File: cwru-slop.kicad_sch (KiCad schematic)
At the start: 58 parts, among them J1 USB_C_Receptacle_USB2.0_16P, J2 FTSH-105-01-L-DV-007-K, J3 Conn_01x03_Pin, J4 54-00320, U1 TLV9001IDCK, U10 B3U-1000P, U11 TLV9001IDCK, U12 TLV9001IDCK, U2 AP63205WU, U3 TLV75533PDBV, U4 STM32L433CCTx, U5 TPS2116DRL, U6 FXLS8974CFR3, U7 ESDCAN24-2BLY, U8 MCP2562-E-SN, U9 24lc32at-i/ot, Y1 XRCGB24M000F3M00R0

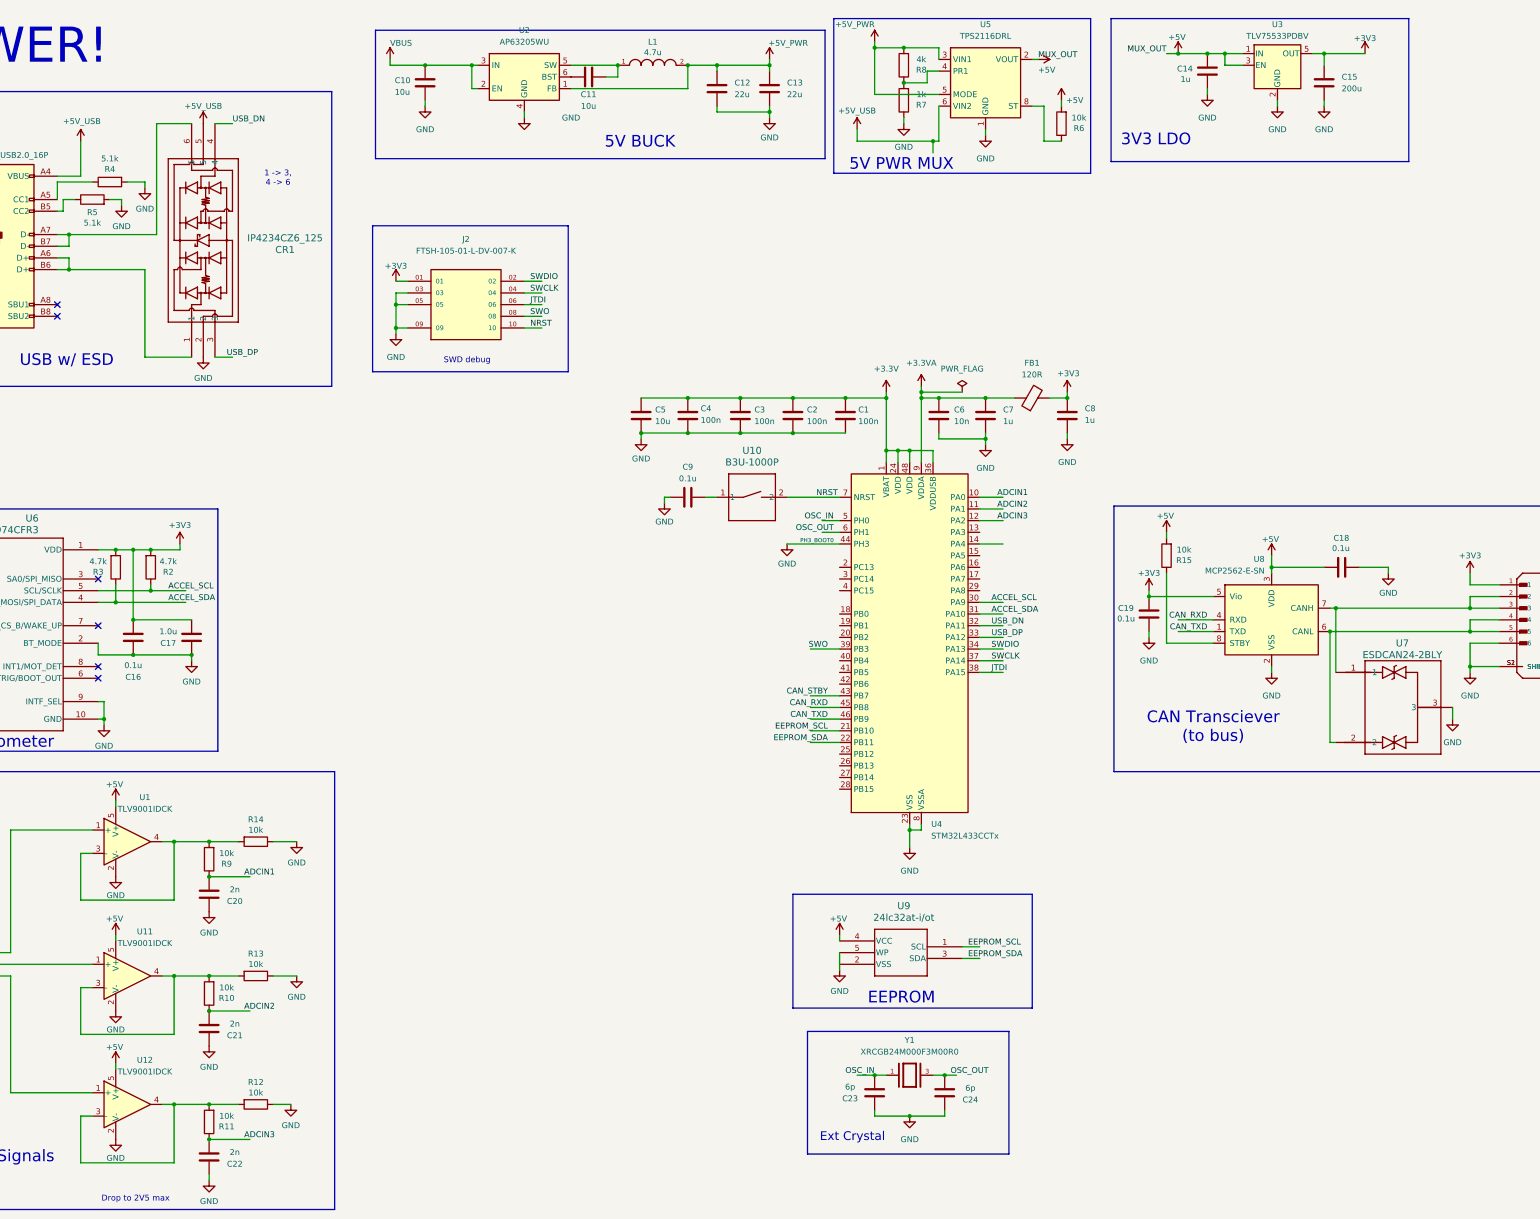
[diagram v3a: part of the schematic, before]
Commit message: add led, pull-ups, clean up a bit
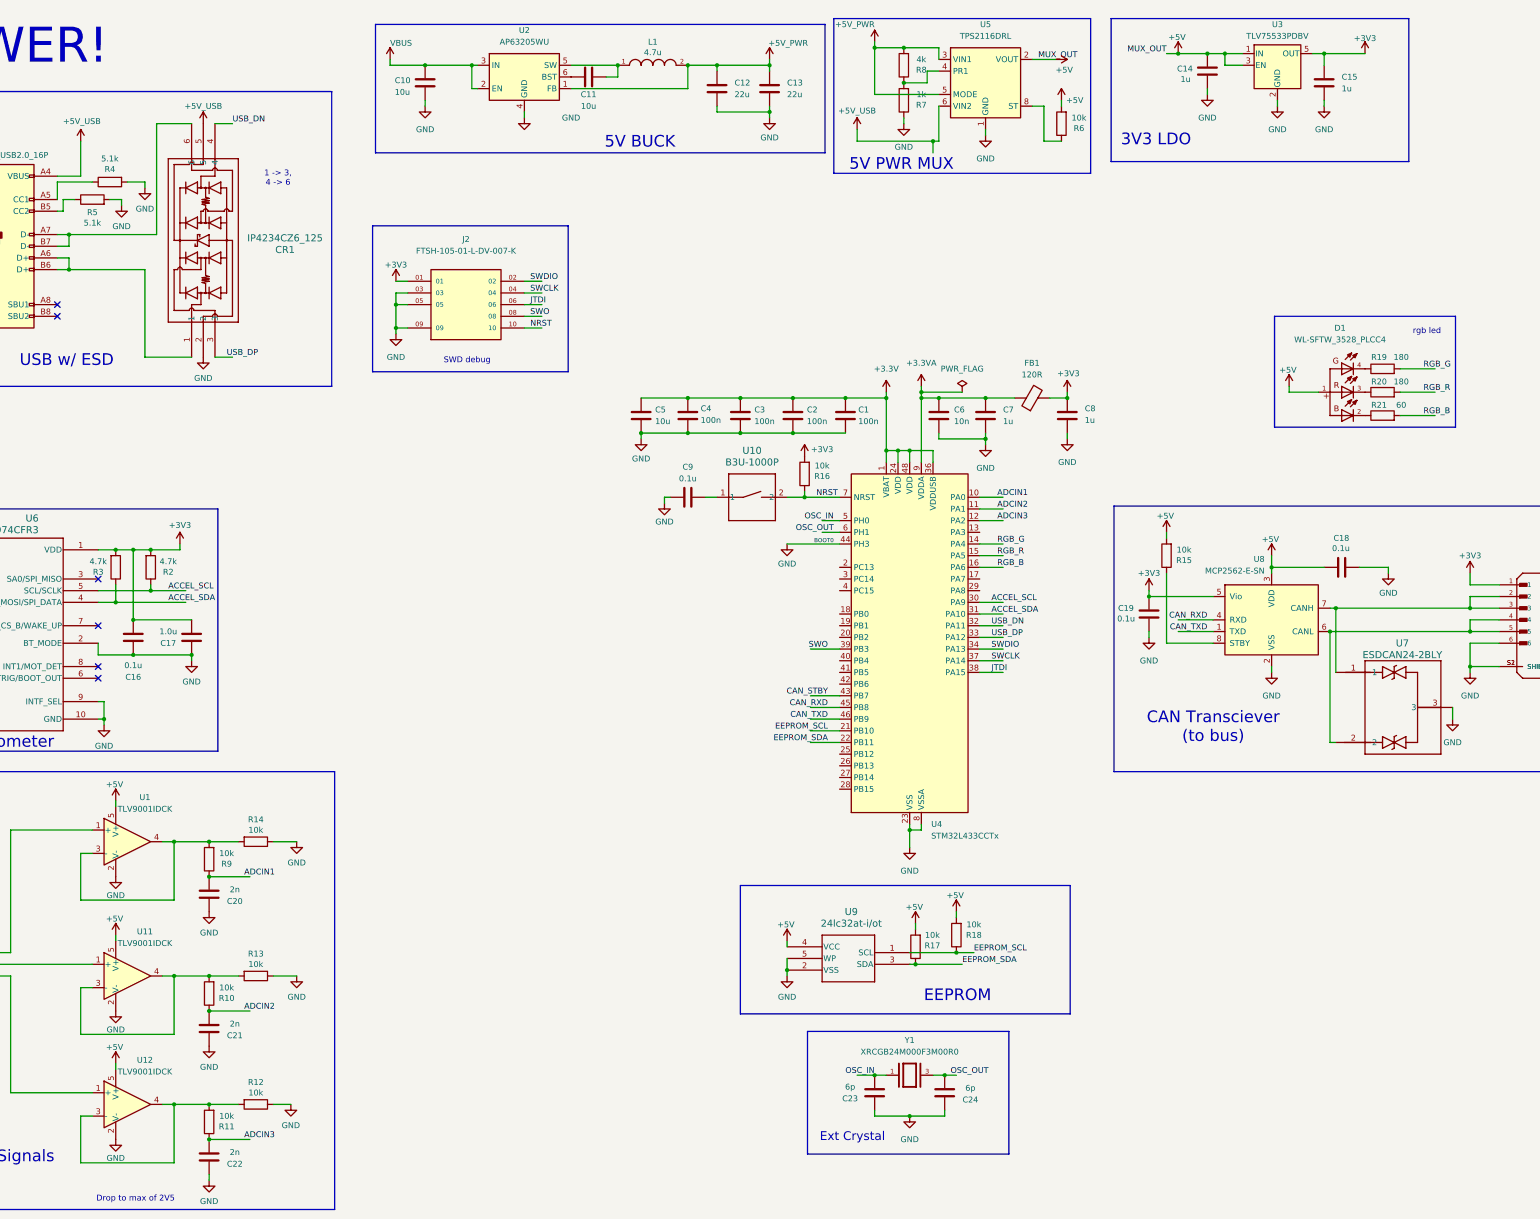
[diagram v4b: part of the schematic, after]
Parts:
- added D1: WL-SFTW_3528_PLCC4, SYS27_Footprints:WL-SFTW_3528_PLCC4, symbol slopp:WL-SFTW_3528_PLCC4
- added R16, R17, R18: 10k, Resistor_SMD:R_0603_1608Metric_Pad0.98x0.95mm_HandSolder, symbol slopp:R
- added R19, R20: 180, Resistor_SMD:R_0603_1608Metric_Pad0.98x0.95mm_HandSolder, symbol slopp:R
- added R21: 60, Resistor_SMD:R_0603_1608Metric_Pad0.98x0.95mm_HandSolder, symbol slopp:R
- C15: value 200u -> 1u
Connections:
- net +3V3: now also R16.2
- net +5V: now also D1.1, R17.2, R18.2
- net EEPROM_SCL: now also R18.1
- net EEPROM_SDA: now also R17.1
- net GND: now also U9.2 (VSS)
- net NRST: now also R16.1
- net RGB_G: now reaches U4.14 (PA4)
- net RGB_G: now also R19.2
- net RGB_R: now reaches U4.15 (PA5)
- net RGB_R: now also R20.2
- net RGB_B: now reaches U4.16 (PA6)
- net RGB_B: now also R21.2
- new net: D1.2, R21.1
- new net: D1.4, R19.1
- new net: D1.3, R20.1
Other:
- note added: "Drop to max of 2V5"
- note added: "rgb led"
- note removed: "Drop to 2V5 max"
- moved on the sheet: U9
